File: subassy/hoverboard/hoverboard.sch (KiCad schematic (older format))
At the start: 2 parts, among them J1 Conn_01x06_MountingPin, J2 Conn_02x05_Odd_Even

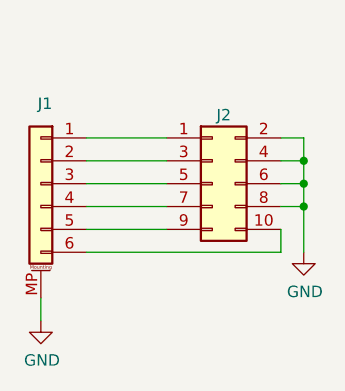
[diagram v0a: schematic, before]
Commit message: Totally messed up the connections to the hoverboard
Great scott!!

Only caught this after placing an order at OSHpark.
Swiftly cancelled for this fix.

Signed-off-by: Michael Welling <mwelling@ieee.org>
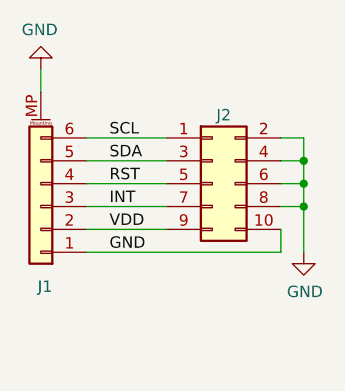
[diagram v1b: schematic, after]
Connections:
- net GND: now also J1.1 (Pin_1), J2.10 (Pin_10)
- net SCL: now reaches J2.1 (Pin_1)
- net SCL: now also J1.6 (Pin_6); no longer J1.1 (Pin_1)
- net SDA: now reaches J2.3 (Pin_3)
- net SDA: now also J1.5 (Pin_5); no longer J1.2 (Pin_2)
- net INT: now reaches J1.3 (Pin_3)
- net INT: now also J2.7 (Pin_7); no longer J2.5 (Pin_5)
- net RST: now reaches J1.4 (Pin_4)
- net RST: now also J2.5 (Pin_5); no longer J2.7 (Pin_7)
- net VDD: now reaches J2.9 (Pin_9)
- net VDD: now also J1.2 (Pin_2); no longer J1.5 (Pin_5)
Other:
- moved on the sheet: J1
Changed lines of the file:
@@
 L Connector_Generic_MountingPin:Conn_01x06_MountingPin J1
 U 1 1 60177A9F
-P 4800 3550
-F 0 "J1" H 4750 3900 50  0000 L CNN
-F 1 "Conn_01x06_MountingPin" H 4888 3373 50  0001 L CNN
-F 2 "kimchi:HRS_FH19C-6S-0.5SH_1x06-1MP_P0.50mm" H 4800 3550 50  0001 C CNN
-F 3 "~" H 4800 3550 50  0001 C CNN
-	1    4800 3550
-	-1   0    0    -1
+P 4800 3650
+F 0 "J1" H 4750 4000 50  0000 L CNN
+F 1 "Conn_01x06_MountingPin" H 4888 3473 50  0001 L CNN
+F 2 "kimchi:HRS_FH19C-6S-0.5SH_1x06-1MP_P0.50mm" H 4800 3650 50  0001 C CNN
+F 3 "~" H 4800 3650 50  0001 C CNN
+	1    4800 3650
+	-1   0    0    1
 $EndComp
 $Comp
@@
 L power:GND #PWR01
 U 1 1 6017B006
-P 4800 4150
-F 0 "#PWR01" H 4800 3900 50  0001 C CNN
-F 1 "GND" H 4805 3977 50  0000 C CNN
-F 2 "" H 4800 4150 50  0001 C CNN
-F 3 "" H 4800 4150 50  0001 C CNN
-	1    4800 4150
-	1    0    0    -1
+P 4800 3050
+F 0 "#PWR01" H 4800 2800 50  0001 C CNN
+F 1 "GND" H 4805 2877 50  0000 C CNN
+F 2 "" H 4800 3050 50  0001 C CNN
+F 3 "" H 4800 3050 50  0001 C CNN
+	1    4800 3050
+	-1   0    0    1
 $EndComp
 $Comp
@@
 	5000 3650 5350 3650
 Wire Wire Line
-	4800 4050 4800 4150
+	4800 3150 4800 3050
 Wire Wire Line
 	5000 3850 5850 3850
 Wire Wire Line
 	5850 3850 5850 3750
+Text Label 5100 3350 0    50   ~ 0
+SCL
+Text Label 5100 3450 0    50   ~ 0
+SDA
+Text Label 5100 3550 0    50   ~ 0
+RST
+Text Label 5100 3650 0    50   ~ 0
+INT
+Text Label 5100 3750 0    50   ~ 0
+VDD
+Text Label 5100 3850 0    50   ~ 0
+GND
 $EndSCHEMATC
